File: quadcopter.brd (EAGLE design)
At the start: 138 x 138 mm, 109 parts, among them J1 AVR_SPI_PRG_6NS, M1 MOTOR_PADS, M2 MOTOR_PADS, M3 MOTOR_PADS, M4 MOTOR_PADS, U1 ATMEGA128RFA1, U2 IMU_LSM9DS1TR, Y1 16MHz

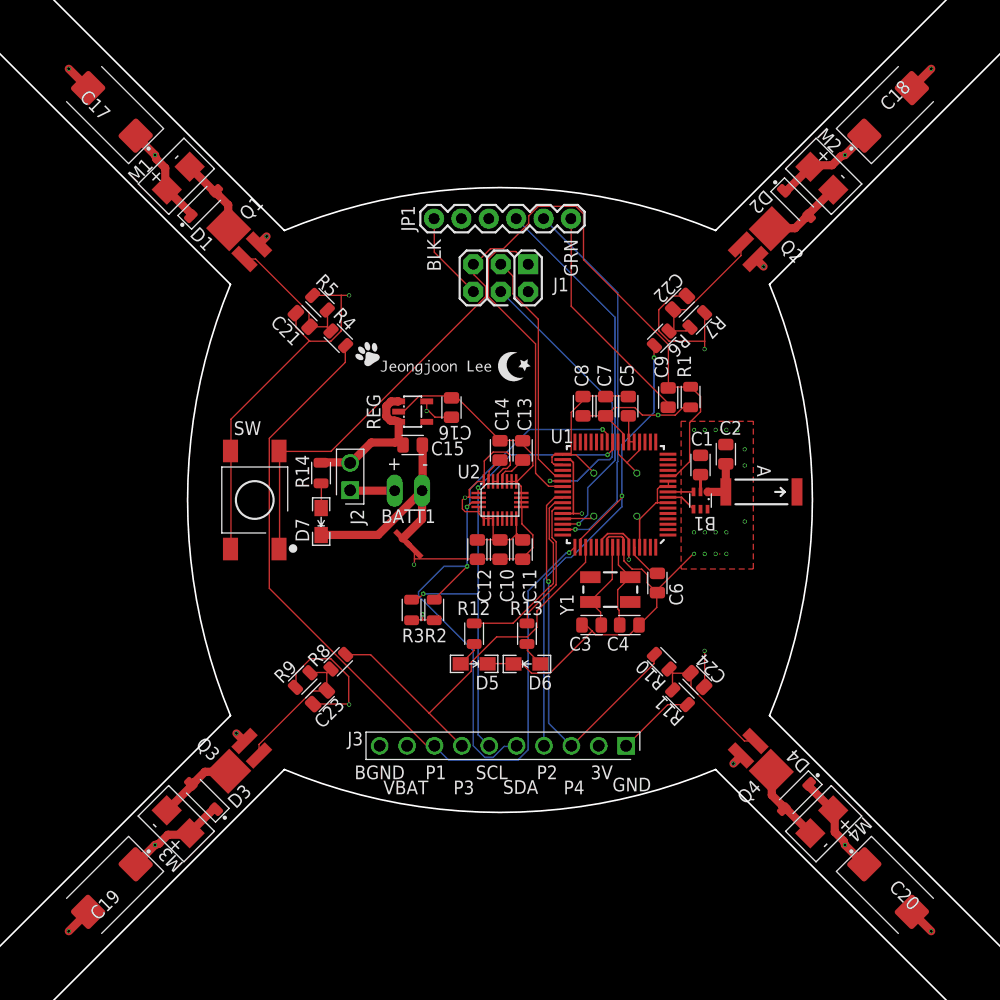
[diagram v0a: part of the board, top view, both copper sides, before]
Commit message: Shink motors components and modified pours
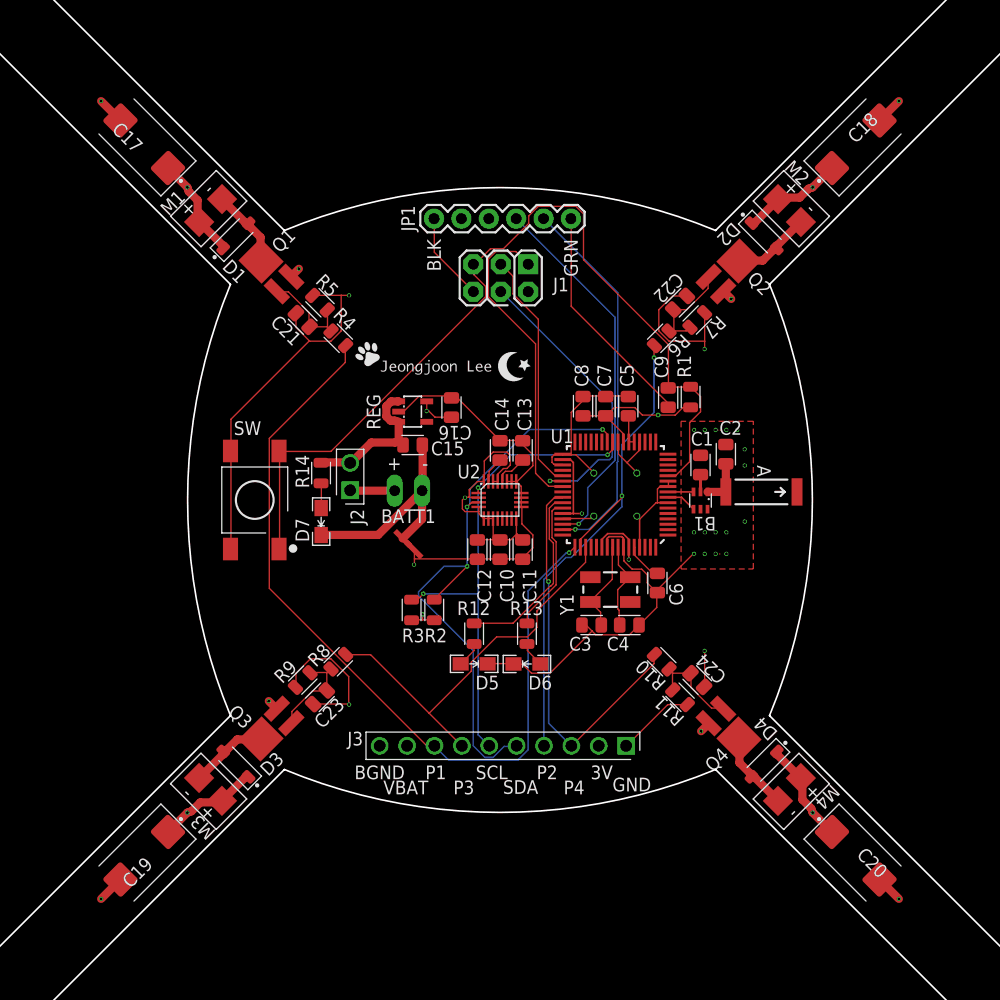
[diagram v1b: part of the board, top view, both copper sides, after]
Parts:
- moved C17 4.24 mm to (-33.0, 33.0)
- moved C18 4.24 mm to (33.0, 33.0)
- moved C19 4.24 mm to (-33.0, -33.0)
- moved C20 4.24 mm to (33.0, -33.0)
- moved D1 4.24 mm to (-24.5, 24.5)
- moved D2 4.24 mm to (24.5, 24.5)
- moved D3 4.24 mm to (-24.5, -24.5)
- moved D4 4.24 mm to (24.5, -24.5)
- moved M1 4.24 mm to (-27.2, 26.5)
- moved M2 4.24 mm to (26.5, 27.2)
- moved M3 4.24 mm to (-26.5, -27.2)
- moved M4 4.24 mm to (27.2, -26.5)
- moved Q1 4.24 mm to (-21.0, 21.0)
- moved Q2 4.24 mm to (21.0, 21.0)
- moved Q3 4.24 mm to (-21.0, -21.0)
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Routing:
- net C22: track 14.0 -> 9.73 mm
- net C24: track 13.1 -> 8.90 mm
- net C23: track 13.1 -> 8.90 mm
- net C21: track 13.1 -> 8.90 mm

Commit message: Finalized version v0.5.0
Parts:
- added STAR1, STAR10, STAR13, STAR14, STAR15, STAR16, STAR17, STAR18, STAR19, STAR20, STAR4, STAR7: (no value), logo:STAR_SCALE_0.1_L21
- added STAR11, STAR2, STAR21, STAR22, STAR23, STAR24, STAR25, STAR26, STAR27, STAR5, STAR8: (no value), logo:STAR_SCALE_0.2_L21
- added STAR12, STAR3, STAR6, STAR9: (no value), logo:STAR_SCALE_0.3_L21
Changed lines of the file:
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@@
 <element name="LOGO1" library="logo" package="LOGO_SCALE_0.9_L21" value="" x="-13.425" y="10.975"/>
 <element name="LOGO2" library="logo" package="LOGO_SCALE_2.0_L22" value="" x="-16" y="-18" rot="R90"/>
+<element name="STAR1" library="logo" package="STAR_SCALE_0.1_L21" value="" x="42.4" y="-42" rot="R180"/>
+<element name="STAR2" library="logo" package="STAR_SCALE_0.2_L21" value="" x="42" y="-39.5" rot="R270"/>
+<element name="STAR3" library="logo" package="STAR_SCALE_0.3_L21" value="" x="42.1" y="-42" rot="R90"/>
+<element name="STAR4" library="logo" package="STAR_SCALE_0.1_L21" value="" x="42" y="42.4" rot="R270"/>
+<element name="STAR5" library="logo" package="STAR_SCALE_0.2_L21" value="" x="39.5" y="42"/>
+<element name="STAR6" library="logo" package="STAR_SCALE_0.3_L21" value="" x="42" y="42.1" rot="R180"/>
+<element name="STAR7" library="logo" package="STAR_SCALE_0.1_L21" value="" x="-42.4" y="42"/>
+<element name="STAR8" library="logo" package="STAR_SCALE_0.2_L21" value="" x="-42" y="39.5" rot="R90"/>
+<element name="STAR9" library="logo" package="STAR_SCALE_0.3_L21" value="" x="-42.1" y="42" rot="R270"/>
+<element name="STAR10" library="logo" package="STAR_SCALE_0.1_L21" value="" x="-42" y="-42.4" rot="R90"/>
+<element name="STAR11" library="logo" package="STAR_SCALE_0.2_L21" value="" x="-39.5" y="-42" rot="R180"/>
+<element name="STAR12" library="logo" package="STAR_SCALE_0.3_L21" value="" x="-42" y="-42.1"/>
+<element name="STAR13" library="logo" package="STAR_SCALE_0.1_L21" value="" x="19.5" y="-10.4" rot="R90"/>
+<element name="STAR14" library="logo" package="STAR_SCALE_0.1_L21" value="" x="-11" y="-4.9" rot="R180"/>
+<element name="STAR15" library="logo" package="STAR_SCALE_0.1_L21" value="" x="-23.8" y="-9.4" rot="R270"/>
+<element name="STAR16" library="logo" package="STAR_SCALE_0.1_L21" value="" x="-7.3" y="-15.8" rot="R270"/>
+<element name="STAR17" library="logo" package="STAR_SCALE_0.1_L21" value="" x="-25" y="10.9"/>
+<element name="STAR18" library="logo" package="STAR_SCALE_0.1_L21" value="" x="-5.4" y="17.3" rot="R180"/>
+<element name="STAR19" library="logo" package="STAR_SCALE_0.1_L21" value="" x="10.9" y="24.8" rot="R270"/>
+<element name="STAR20" library="logo" package="STAR_SCALE_0.1_L21" value="" x="23.4" y="11.2" rot="R180"/>
+<element name="STAR21" library="logo" package="STAR_SCALE_0.2_L21" value="" x="-13.2" y="-9" rot="R270"/>
+<element name="STAR22" library="logo" package="STAR_SCALE_0.2_L21" value="" x="-15.2" y="9.2" rot="R90"/>
+<element name="STAR23" library="logo" package="STAR_SCALE_0.2_L21" value="" x="7.4" y="14.3"/>
+<element name="STAR24" library="logo" package="STAR_SCALE_0.2_L21" value="" x="-12.8" y="25.1" rot="R180"/>
+<element name="STAR25" library="logo" package="STAR_SCALE_0.2_L21" value="" x="24.1" y="-10.5" rot="R270"/>
+<element name="STAR26" library="logo" package="STAR_SCALE_0.2_L21" value="" x="2.3" y="-18.7" rot="R270"/>
+<element name="STAR27" library="logo" package="STAR_SCALE_0.2_L21" value="" x="-14.8" y="-24.3" rot="R90"/>
 </elements>
 <signals>

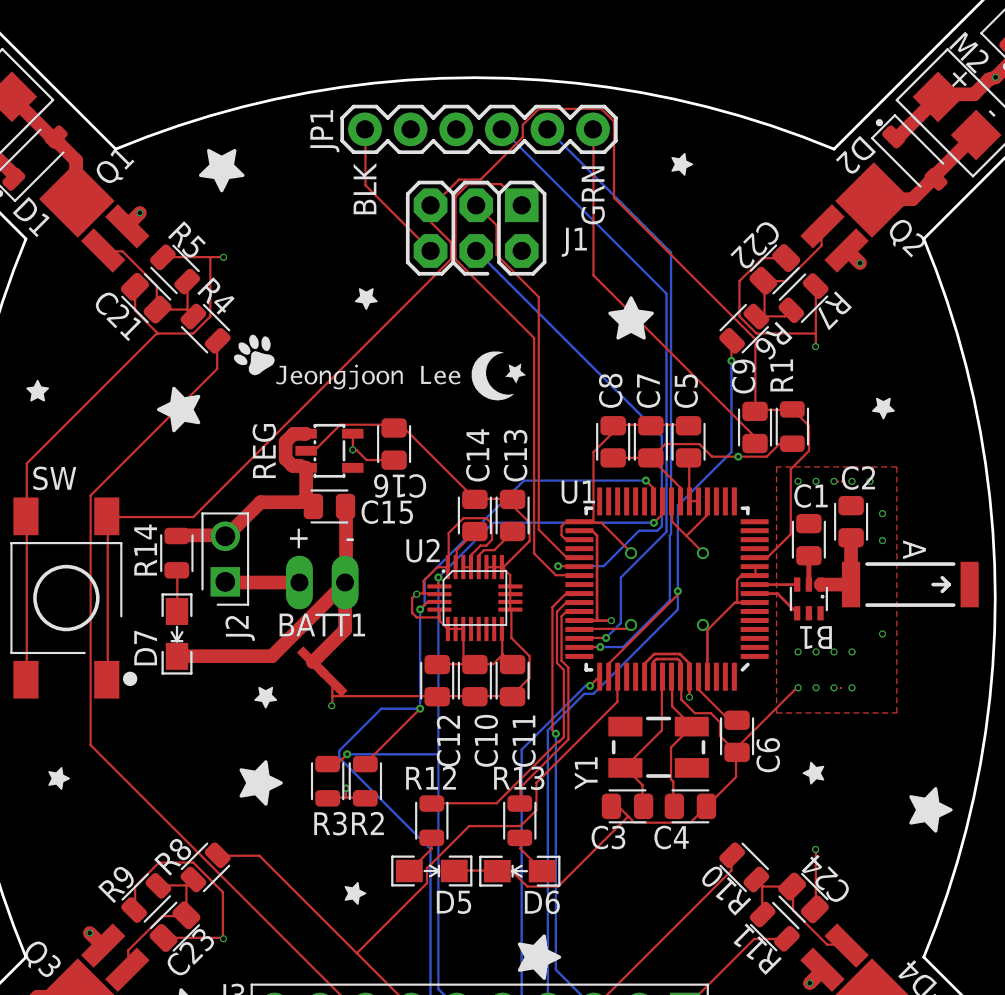
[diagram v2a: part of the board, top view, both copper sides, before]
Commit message: Shrink antenna driver pour
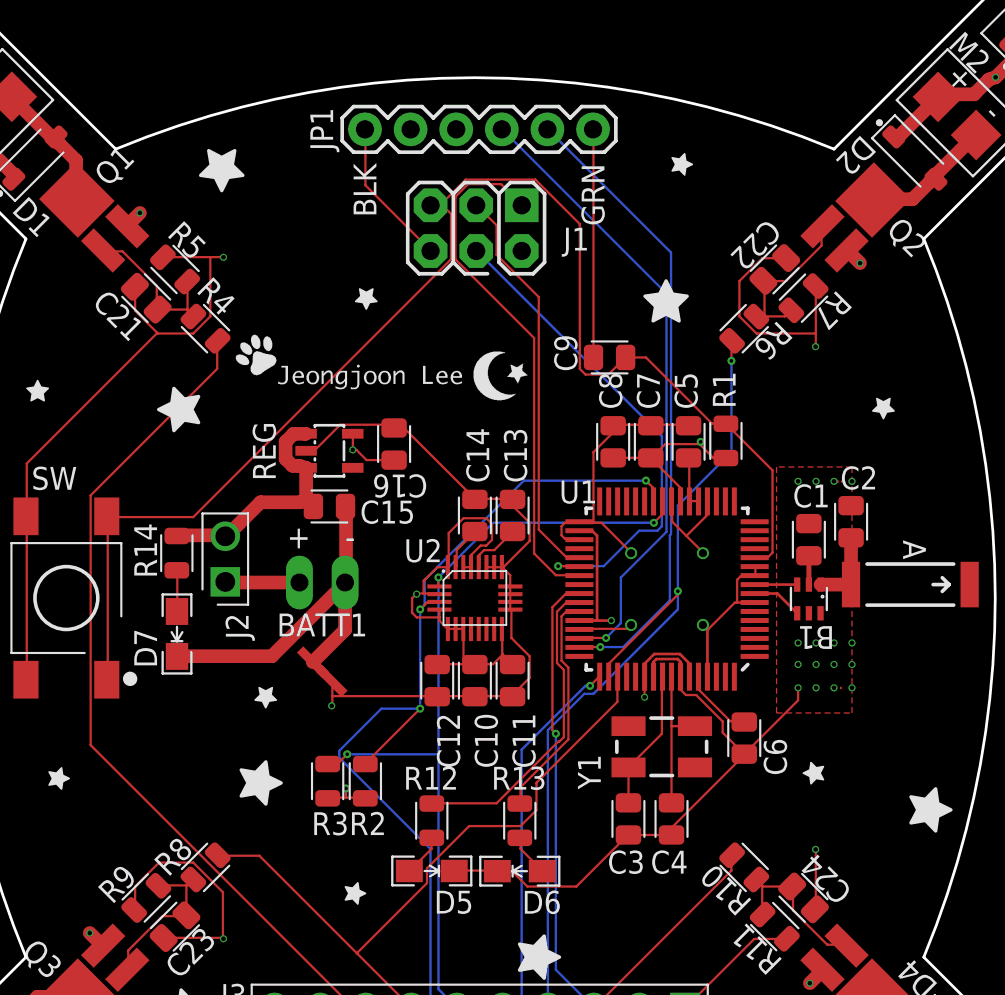
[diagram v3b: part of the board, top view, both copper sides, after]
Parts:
- moved V17 10.2 mm to (21.0, -3.70)
- moved V25 9.63 mm to (18.0, -3.70)
- moved C9 8.99 mm to (7.50, 13.4), turned to 0 degrees
- moved V26 7.83 mm to (19.0, -3.70)
- moved R1 3.79 mm to (14.0, 8.75)
- moved V27 3.19 mm to (20.0, -3.70)
- moved V37 2.50 mm to (9.45, -5.52)
- moved STAR23 2.17 mm to (9.35, 15.2)
- moved C4 1.26 mm to (10.9, -12.3), turned to 270 degrees
- moved C3 0.70 mm to (8.55, -12.3), turned to 270 degrees
- moved V13 0.50 mm to (18.0, -2.50)
- moved V14 0.50 mm to (19.0, -2.50)
- moved V15 0.50 mm to (20.0, -2.50)
- moved V16 0.50 mm to (21.0, -2.50)
- moved C6 0.41 mm to (15.0, -7.80)
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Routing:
- net C9: track 21.2 -> 12.7 mm
- net RESET: track 82.8 -> 75.7 mm
- net 3V: track 58.9 -> 55.9 mm
- net GND: track 191.5 -> 190.4 mm
- net C3: track 8.52 -> 7.83 mm
